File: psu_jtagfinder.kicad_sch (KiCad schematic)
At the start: 0 parts

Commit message: [WIP] PSU stage
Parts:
- added C11, C12, C14: 10uF, symbol Device:C
- added C13: 100nF, symbol Device:C
- added D1: D_Schottky, symbol Device:D_Schottky
- added L2: 15uH, symbol Device:L
- added R6: 10k, symbol Device:R
- added U3: MIC2025-2YM, Package_SO:SOIC-8_3.9x4.9mm_P1.27mm, symbol Power_Management:MIC2025-2YM
- added U5: TLV74033, Package_TO_SOT_SMD:SOT-23-5, symbol LDO:TLV74033PDBVR
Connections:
- new net: C12.1, D1.1 (K), L2.2, R6.1, U5.1 (IN)
- new net: C13.1, R6.2, U5.3 (EN)
- new net +3.3V: C14.1, D1.2 (A), U5.5 (OUT)
- new net +5V: C11.1, L2.1, U3.6 (OUT), U3.8 (OUT)
- new net GND: C11.2, C12.2, C13.2, C14.2, U3.3 (GND), U5.2 (GND)
- new net VCC: U3.7 (IN)
- new net ~EN_MIC2025: U3.1 (EN)
- no-connect marks 0 -> 1

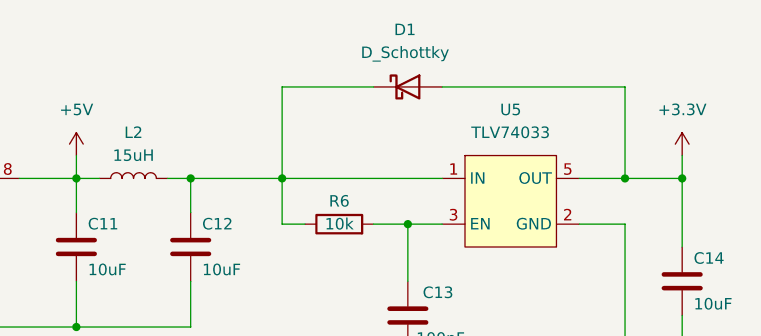
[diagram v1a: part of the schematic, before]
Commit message: [ADD] comments and esd protection
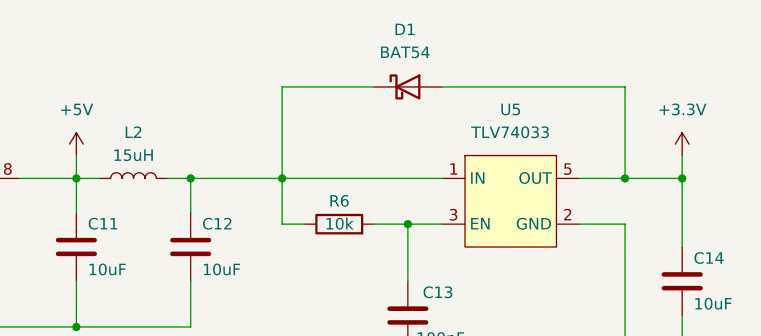
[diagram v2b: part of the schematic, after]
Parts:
- D1: value D_Schottky -> BAT54; footprint (none) -> Diode_SMD:D_SOD-323_HandSoldering; Man.: (none) -> DIODES; Ref. Man. (none) -> BAT54WS
- L2: footprint (none) -> Inductors_SMD:L_1.4x5.0mm_CM45_BOURNS_Series
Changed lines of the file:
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@@
       (effects (font (size 1.27 1.27)))
     )
-    (property "Value" "D_Schottky" (at 120.3325 29.21 0)
+    (property "Value" "BAT54" (at 120.3325 29.21 0)
       (effects (font (size 1.27 1.27)))
     )
-    (property "Footprint" "" (at 120.65 33.02 0)
+    (property "Footprint" "Diode_SMD:D_SOD-323_HandSoldering" (at 120.65 33.02 0)
       (effects (font (size 1.27 1.27)) hide)
     )
-    (property "Datasheet" "~" (at 120.65 33.02 0)
+    (property "Datasheet" "https://www.mouser.es/datasheet/2/115/DIOD_S_A0004140728_1-2542383.pdf" (at 120.65 33.02 0)
+      (effects (font (size 1.27 1.27)) hide)
+    )
+    (property "Man.:" "DIODES" (at 120.65 33.02 0)
+      (effects (font (size 1.27 1.27)) hide)
+    )
+    (property "Ref. Man." "BAT54WS" (at 120.65 33.02 0)
       (effects (font (size 1.27 1.27)) hide)
     )
@@
       (effects (font (size 1.27 1.27)))
     )
-    (property "Footprint" "" (at 90.17 43.18 0)
+    (property "Footprint" "Inductors_SMD:L_1.4x5.0mm_CM45_BOURNS_Series" (at 90.17 43.18 0)
       (effects (font (size 1.27 1.27)) hide)
     )

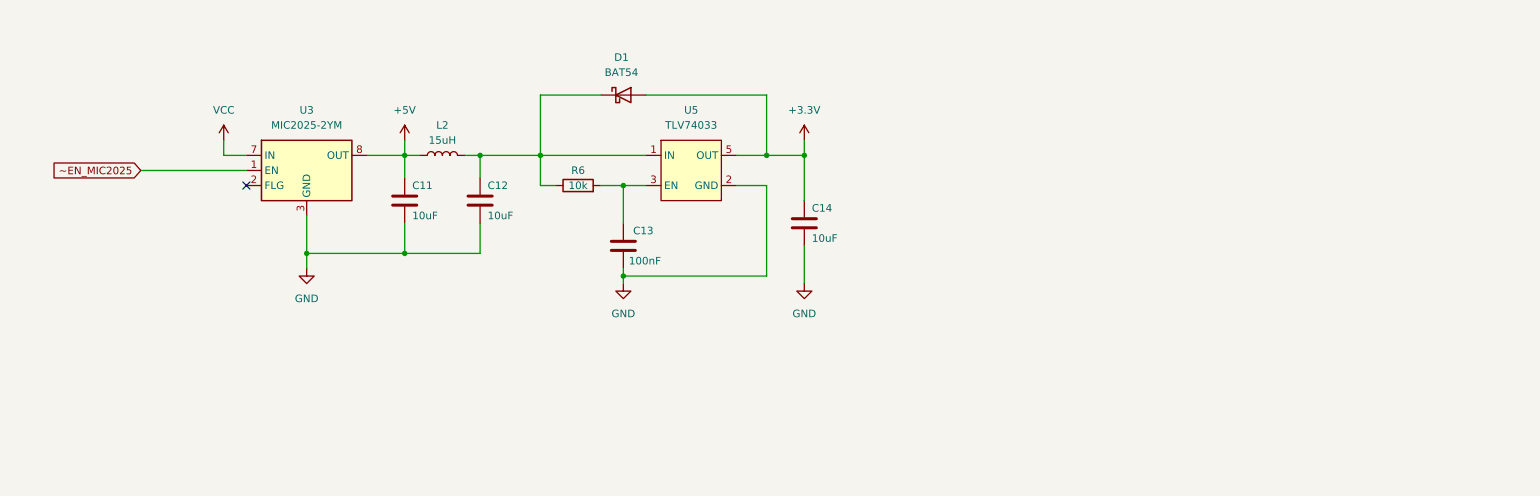
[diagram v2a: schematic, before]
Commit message: [FIX] ERC failure, add sheets for output stage
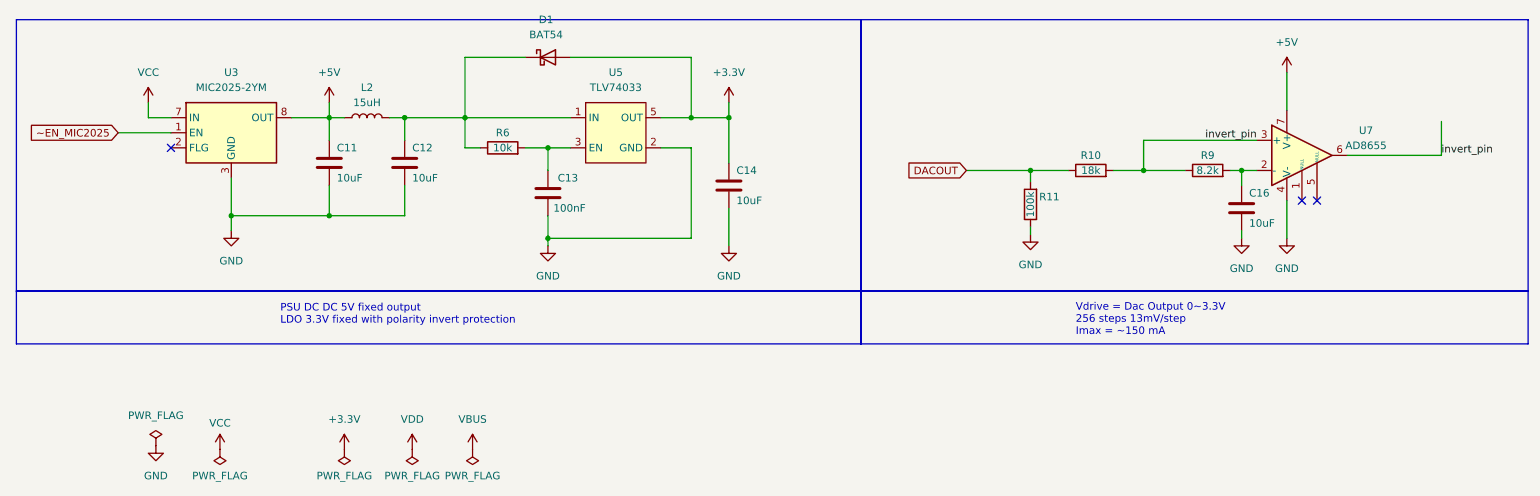
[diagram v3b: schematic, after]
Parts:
- added C16: 10uF, symbol Device:C
- added R10: 18k, symbol Device:R
- added R11: 100k, symbol Device:R
- added R9: 8.2k, symbol Device:R
- added U7: AD8655, symbol Amplifier_Operational:AD8655
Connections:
- net +5V: now also U7.7 (V+)
- net GND: now also C16.2, R11.1, U7.4 (V-)
- new net: C16.1, R9.2, U7.2 (-)
- new net DACOUT: R10.1, R11.2
- new net invert_pin: R10.2, R9.1, U7.3 (+), U7.6
- no-connect marks 1 -> 3
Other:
- note added: "PSU DC DC 5V fixed output LDO 3.3V fixed with polarity invert protection"
- note added: "Vdrive = Dac Output 0~3.3V 256 steps 13mV/step Imax = ~150 mA"
- moved on the sheet: C11, C12, C13, C14, D1, L2, R6, U3, U5

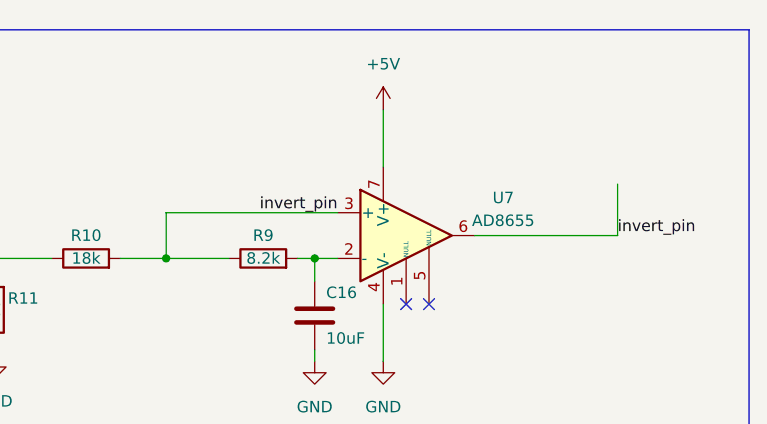
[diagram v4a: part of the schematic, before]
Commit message: [WIP] pcb design with minor fixes in schema to have cleanest routing
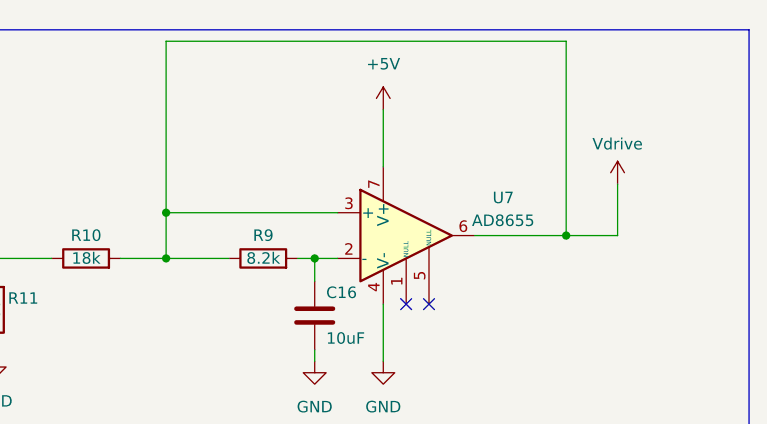
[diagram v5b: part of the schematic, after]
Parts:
- C11, C12, C14, C16: footprint (none) -> Capacitor_SMD:CP_Elec_4x5.4; Fab: (none) -> KNSCHA; Man #: (none) -> RST10UF25V014
- C13: footprint (none) -> Capacitor_SMD:C_1206_3216Metric; Fab: (none) -> Yageo; Man #: (none) -> CC1206KKX7RCBB103
- D1: footprint Diode_SMD:D_SOD-323_HandSoldering -> Diode_SMD:D_SOD-323; Fab: (none) -> DIODES; Man #: (none) -> BAT54WS
- L2: Fab: (none) -> Bourns; Man #: (none) -> CM453232-150KL
- R10: footprint (none) -> Resistor_SMD:R_1206_3216Metric; Fab: (none) -> VO; Man #: (none) -> SCR1206J18K
- R11: footprint (none) -> Resistor_SMD:R_1206_3216Metric; Fab: (none) -> FOJAN; Man #: (none) -> FRC1206J104 TS
- R6: footprint (none) -> Resistor_SMD:R_1206_3216Metric; Fab: (none) -> VO; Man #: (none) -> SCR1206J10K
- R9: footprint (none) -> Resistor_SMD:R_1206_3216Metric; Fab: (none) -> FOJAN; Man #: (none) -> FRC1206J822 TS
- U5: Fab: (none) -> Texas Instrument
- U7: footprint (none) -> Package_SO:SOIC-8-1EP_3.9x4.9mm_P1.27mm_EP2.29x3mm
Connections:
- net invert_pin renamed Vdrive
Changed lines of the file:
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@@
   (junction (at 107.95 57.15) (diameter 0) (color 0 0 0 0)
   )
+  (junction (at 252.73 43.18) (diameter 0) (color 0 0 0 0)
+  )
   (junction (at 224.79 45.72) (diameter 0) (color 0 0 0 0)
   )
@@
   )
   (junction (at 132.08 36.83) (diameter 0) (color 0 0 0 0)
+  )
+  (junction (at 208.28 40.64) (diameter 0) (color 0 0 0 0)
   )
   (junction (at 83.82 36.83) (diameter 0) (color 0 0 0 0)
@@
     (stroke (width 0) (type default))
   )
+  (wire (pts (xy 252.73 43.18) (xy 252.73 21.59))
+    (stroke (width 0) (type default))
+  )
   (wire (pts (xy 93.98 36.83) (xy 93.98 41.91))
     (stroke (width 0) (type default))
@@
     (stroke (width 0) (type default))
   )
-  (wire (pts (xy 242.57 43.18) (xy 258.445 43.18))
-    (stroke (width 0) (type default))
-  )
   (wire (pts (xy 189.23 45.72) (xy 195.58 45.72))
     (stroke (width 0) (type default))
@@
     (stroke (width 0) (type default))
   )
+  (wire (pts (xy 242.57 43.18) (xy 252.73 43.18))
+    (stroke (width 0) (type default))
+  )
   (wire (pts (xy 227.33 40.64) (xy 208.28 40.64))
     (stroke (width 0) (type default))
   )
+  (wire (pts (xy 208.28 21.59) (xy 208.28 40.64))
+    (stroke (width 0) (type default))
+  )
   (wire (pts (xy 71.12 40.64) (xy 71.12 36.83))
     (stroke (width 0) (type default))
@@
     (stroke (width 0) (type default))
   )
+  (wire (pts (xy 252.73 43.18) (xy 258.445 43.18))
+    (stroke (width 0) (type default))
+  )
   (wire (pts (xy 83.82 36.83) (xy 83.82 40.64))
+    (stroke (width 0) (type default))
+  )
+  (wire (pts (xy 252.73 21.59) (xy 208.28 21.59))
     (stroke (width 0) (type default))
   )
@@
     (at 62.865 71.755 0)
     (effects (font (size 1.27 1.27)) (justify left bottom))
-  )
-  (label "invert_pin" (at 258.445 43.18 0) (fields_autoplaced)
-    (effects (font (size 1.27 1.27)) (justify left bottom))
-  )
-  (label "invert_pin" (at 227.33 40.64 180) (fields_autoplaced)
-    (effects (font (size 1.27 1.27)) (justify right bottom))
   )
   (global_label "DACOUT" (shape input) (at 178.435 45.72 180) (fields_autoplaced)
@@
       (effects (font (size 1.27 1.27)) (justify left))
     )
-    (property "Footprint" "" (at 84.7852 48.26 0)
+    (property "Footprint" "Capacitor_SMD:CP_Elec_4x5.4" (at 84.7852 48.26 0)
       (effects (font (size 1.27 1.27)) hide)
     )
@@
       (effects (font (size 1.27 1.27)) hide)
     )
+    (property "Man #:" "RST10UF25V014" (at 83.82 44.45 0)
+      (effects (font (size 1.27 1.27)) hide)
+    )
+    (property "Fab:" "KNSCHA" (at 83.82 44.45 0)
+      (effects (font (size 1.27 1.27)) hide)
+    )
     (pin "1")
     (pin "2")
@@
     )
     (property "Man.:" "Texas Instrument" (at 119.38 52.07 0)
+      (effects (font (size 1.27 1.27)) hide)
+    )
+    (property "Man #:" "" (at 119.38 39.37 0)
+      (effects (font (size 1.27 1.27)) hide)
+    )
+    (property "Fab:" "Texas Instrument" (at 119.38 39.37 0)
       (effects (font (size 1.27 1.27)) hide)
     )
@@
       (effects (font (size 1.27 1.27)))
     )
-    (property "Footprint" "" (at 100.33 43.688 90)
+    (property "Footprint" "Resistor_SMD:R_1206_3216Metric" (at 100.33 43.688 90)
       (effects (font (size 1.27 1.27)) hide)
     )
@@
       (effects (font (size 1.27 1.27)) hide)
     )
+    (property "Man #:" "SCR1206J10K" (at 100.33 41.91 0)
+      (effects (font (size 1.27 1.27)) hide)
+    )
+    (property "Fab:" "VO" (at 100.33 41.91 0)
+      (effects (font (size 1.27 1.27)) hide)
+    )
     (pin "1")
     (pin "2")
@@
         (path "/204d557f-3c83-43db-b1fd-628e15efe3d8/651e631a-de0f-4a69-a119-5cdead14cfb1"
           (reference "R6") (unit 1)
+        )
+      )
+    )
+  )
+  (symbol (lib_id "power:Vdrive") (at 258.445 37.465 0) (unit 1)
+    (in_bom yes) (on_board yes) (dnp no) (fields_autoplaced)
+    (property "Reference" "#PWR096" (at 253.365 41.275 0)
+      (effects (font (size 1.27 1.27)) hide)
+    )
+    (property "Value" "Vdrive" (at 258.445 33.02 0)
+      (effects (font (size 1.27 1.27)))
+    )
+    (property "Footprint" "" (at 258.445 37.465 0)
+      (effects (font (size 1.27 1.27)) hide)
+    )
+    (property "Datasheet" "" (at 258.445 37.465 0)
+      (effects (font (size 1.27 1.27)) hide)
+    )
+    (pin "1")
+    (instances
+      (project "JTAGFinder"
+        (path "/204d557f-3c83-43db-b1fd-628e15efe3d8/651e631a-de0f-4a69-a119-5cdead14cfb1"
+          (reference "#PWR096") (unit 1)
         )
       )
@@
       (effects (font (size 1.27 1.27)) (justify left))
     )
-    (property "Footprint" "" (at 139.3952 52.07 0)
+    (property "Footprint" "Capacitor_SMD:CP_Elec_4x5.4" (at 139.3952 52.07 0)
       (effects (font (size 1.27 1.27)) hide)
     )
     (property "Datasheet" "~" (at 138.43 48.26 0)
+      (effects (font (size 1.27 1.27)) hide)
+    )
+    (property "Man #:" "RST10UF25V014" (at 138.43 48.26 0)
+      (effects (font (size 1.27 1.27)) hide)
+    )
+    (property "Fab:" "KNSCHA" (at 138.43 48.26 0)
       (effects (font (size 1.27 1.27)) hide)
     )
@@
       (effects (font (size 1.27 1.27)) (justify left))
     )
-    (property "Footprint" "" (at 72.0852 48.26 0)
+    (property "Footprint" "Capacitor_SMD:CP_Elec_4x5.4" (at 72.0852 48.26 0)
       (effects (font (size 1.27 1.27)) hide)
     )
     (property "Datasheet" "~" (at 71.12 44.45 0)
+      (effects (font (size 1.27 1.27)) hide)
+    )
+    (property "Man #:" "RST10UF25V014" (at 71.12 44.45 0)
+      (effects (font (size 1.27 1.27)) hide)
+    )
+    (property "Fab:" "KNSCHA" (at 71.12 44.45 0)
       (effects (font (size 1.27 1.27)) hide)
     )
@@
       (effects (font (size 1.27 1.27)) (justify left))
     )
-    (property "Footprint" "" (at 225.7552 55.88 0)
+    (property "Footprint" "Capacitor_SMD:CP_Elec_4x5.4" (at 225.7552 55.88 0)
       (effects (font (size 1.27 1.27)) hide)
     )
@@
       (effects (font (size 1.27 1.27)) hide)
     )
+    (property "Man #:" "RST10UF25V014" (at 224.79 52.07 0)
+      (effects (font (size 1.27 1.27)) hide)
+    )
+    (property "Fab:" "KNSCHA" (at 224.79 52.07 0)
+      (effects (font (size 1.27 1.27)) hide)
+    )
     (pin "1")
     (pin "2")
@@
       (effects (font (size 1.27 1.27)))
     )
-    (property "Footprint" "" (at 236.22 41.91 0)
+    (property "Footprint" "Package_SO:SOIC-8-1EP_3.9x4.9mm_P1.27mm_EP2.29x3mm" (at 236.22 41.91 0)
       (effects (font (size 1.27 1.27)) hide)
     )
     (property "Datasheet" "https://www.analog.com/media/en/technical-documentation/data-sheets/ad8655_8656.pdf" (at 238.76 39.37 0)
+      (effects (font (size 1.27 1.27)) hide)
+    )
+    (property "Man #:" "" (at 234.95 43.18 0)
       (effects (font (size 1.27 1.27)) hide)
     )
@@
       (effects (font (size 1.27 1.27)) hide)
     )
+    (property "Man #:" "" (at 54.61 39.37 0)
+      (effects (font (size 1.27 1.27)) hide)
+    )
     (pin "1")
     (pin "2")
@@
       (effects (font (size 1.27 1.27)))
     )
-    (property "Footprint" "" (at 219.075 47.498 90)
+    (property "Footprint" "Resistor_SMD:R_1206_3216Metric" (at 219.075 47.498 90)
       (effects (font (size 1.27 1.27)) hide)
     )
     (property "Datasheet" "~" (at 219.075 45.72 0)
+      (effects (font (size 1.27 1.27)) hide)
+    )
+    (property "Man #:" "FRC1206J822 TS" (at 219.075 45.72 0)
+      (effects (font (size 1.27 1.27)) hide)
+    )
+    (property "Fab:" "FOJAN" (at 219.075 45.72 0)
       (effects (font (size 1.27 1.27)) hide)
     )
@@
       (effects (font (size 1.27 1.27)) (justify left))
     )
-    (property "Footprint" "" (at 106.9848 53.34 0)
+    (property "Footprint" "Capacitor_SMD:C_1206_3216Metric" (at 106.9848 53.34 0)
       (effects (font (size 1.27 1.27)) hide)
     )
@@
       (effects (font (size 1.27 1.27)) hide)
     )
+    (property "Man #:" "CC1206KKX7RCBB103" (at 107.95 49.53 0)
+      (effects (font (size 1.27 1.27)) hide)
+    )
+    (property "Fab:" "Yageo" (at 107.95 49.53 0)
+      (effects (font (size 1.27 1.27)) hide)
+    )
     (pin "1")
     (pin "2")
@@
       (effects (font (size 1.27 1.27)))
     )
-    (property "Footprint" "Diode_SMD:D_SOD-323_HandSoldering" (at 107.95 26.67 0)
+    (property "Footprint" "Diode_SMD:D_SOD-323" (at 107.95 26.67 0)
       (effects (font (size 1.27 1.27)) hide)
     )
@@
     )
     (property "Ref. Man." "BAT54WS" (at 107.95 26.67 0)
+      (effects (font (size 1.27 1.27)) hide)
+    )
+    (property "Man #:" "BAT54WS" (at 107.95 26.67 0)
+      (effects (font (size 1.27 1.27)) hide)
+    )
+    (property "Fab:" "DIODES" (at 107.95 26.67 0)
       (effects (font (size 1.27 1.27)) hide)
     )
@@
       (effects (font (size 1.27 1.27)))
     )
-    (property "Footprint" "" (at 199.39 47.498 90)
+    (property "Footprint" "Resistor_SMD:R_1206_3216Metric" (at 199.39 47.498 90)
       (effects (font (size 1.27 1.27)) hide)
     )
@@
       (effects (font (size 1.27 1.27)) hide)
     )
+    (property "Man #:" "SCR1206J18K" (at 199.39 45.72 0)
+      (effects (font (size 1.27 1.27)) hide)
+    )
+    (property "Fab:" "VO" (at 199.39 45.72 0)
+      (effects (font (size 1.27 1.27)) hide)
+    )
     (pin "1")
     (pin "2")
@@
     )
     (property "Man.:" "Bourns" (at 77.47 36.83 90)
+      (effects (font (size 1.27 1.27)) hide)
+    )
+    (property "Man #:" "CM453232-150KL" (at 77.47 36.83 0)
+      (effects (font (size 1.27 1.27)) hide)
+    )
+    (property "Fab:" "Bourns" (at 77.47 36.83 0)
       (effects (font (size 1.27 1.27)) hide)
     )
@@
       (effects (font (size 1.27 1.27)))
     )
-    (property "Footprint" "" (at 191.008 51.435 90)
+    (property "Footprint" "Resistor_SMD:R_1206_3216Metric" (at 191.008 51.435 90)
       (effects (font (size 1.27 1.27)) hide)
     )
@@
       (effects (font (size 1.27 1.27)) hide)
     )
+    (property "Man #:" "FRC1206J104 TS" (at 189.23 51.435 0)
+      (effects (font (size 1.27 1.27)) hide)
+    )
+    (property "Fab:" "FOJAN" (at 189.23 51.435 0)
+      (effects (font (size 1.27 1.27)) hide)
+    )
